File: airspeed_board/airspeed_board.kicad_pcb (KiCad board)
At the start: 2 copper layers, 6 parts, among them J1 BME280, J2 ADXL345, J3 MPXV5002DP, U1 ESP32-C3_SUPERMINI, U2 XGZP6897D_1, U3 XGZP6897D_2

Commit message: updated board layout
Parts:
- removed J3: MPXV5002DP, Connector_PinHeader_2.54mm:PinHeader_1x03_P2.54mm_Vertical
- added C1: 0.1uF, Capacitor_SMD:C_0805_2012Metric, F.Cu at (147.0, 80.3)
- J1: moved to B.Cu
- moved U3 14.9 mm to (138.9, 71.1), turned to 0 degrees
- moved J2 13.8 mm to (168.3, 76.8)
- moved U2 10.0 mm to (138.9, 59.2), turned to 0 degrees
- moved U1 4.66 mm to (138.9, 65.4), turned to 180 degrees
- moved J1 4.47 mm to (150.2, 55.6), turned to -90 degrees
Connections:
- J1 pad 1: unconnected-(J1-Pin_1-Pad1) -> 3.3V
- J1 pad 2: unconnected-(J1-Pin_2-Pad2) -> GND
- J1 pad 3: unconnected-(J1-Pin_3-Pad3) -> SCL
- J1 pad 4: unconnected-(J1-Pin_4-Pad4) -> SDA
- J2 pad 1: unconnected-(J2-Pin_1-Pad1) -> GND
- J2 pad 2: unconnected-(J2-Pin_2-Pad2) -> 3.3V
- J2 pad 7: unconnected-(J2-Pin_7-Pad7) -> SDA
- J2 pad 8: unconnected-(J2-Pin_8-Pad8) -> SCL
- U1 pad 5V: unconnected-(U1-Pad5V) -> 5V
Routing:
- net 3.3V: track 14.9 -> 81.5 mm
- net SCL: track 17.8 -> 62.5 mm, vias 0 -> 1
- net SDA: track 20.6 -> 51.2 mm, vias 0 -> 1
- net GND: track 26.9 -> 0.00 mm
- added copper zone on B.Cu, net GND
- added copper zone on F.Cu, net GND
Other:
- board outline added: 49.5 x 31.2 mm

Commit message: updates to pcb
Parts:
- removed C1: 0.1uF, Capacitor_SMD:C_0805_2012Metric
- moved U3 13.0 mm to (138.9, 58.2)
- moved U2 11.4 mm to (138.9, 70.6)
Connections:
- U1 pad 20: unconnected-(U1-GPIO20-Pad20) -> SDA2
- U1 pad 21: unconnected-(U1-GPIO21-Pad21) -> SCL2
- U3 pad 6: SDA -> SDA2
- U3 pad 7: SCL -> SCL2
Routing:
- net SCL2: track 0.00 -> 19.7 mm
- net SDA: track 51.2 -> 32.3 mm, vias 1 -> 0
- net SCL: track 62.5 -> 47.7 mm, vias 1 -> 0
- net 3.3V: track 81.5 -> 73.5 mm, vias 0 -> 1
- net SDA2: track 0.00 -> 4.41 mm
- removed copper zone on F.Cu, net GND
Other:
- board size 49.5 x 31.2 mm -> 47 x 29.7 mm
- board text added: "SCL"
- board text added: "SCL2"
- board text added: "SDA"
- board text added: "SDA2"
- board text added: "niig:2024.03.04"
- board text added: "velometa.com/airspeed"

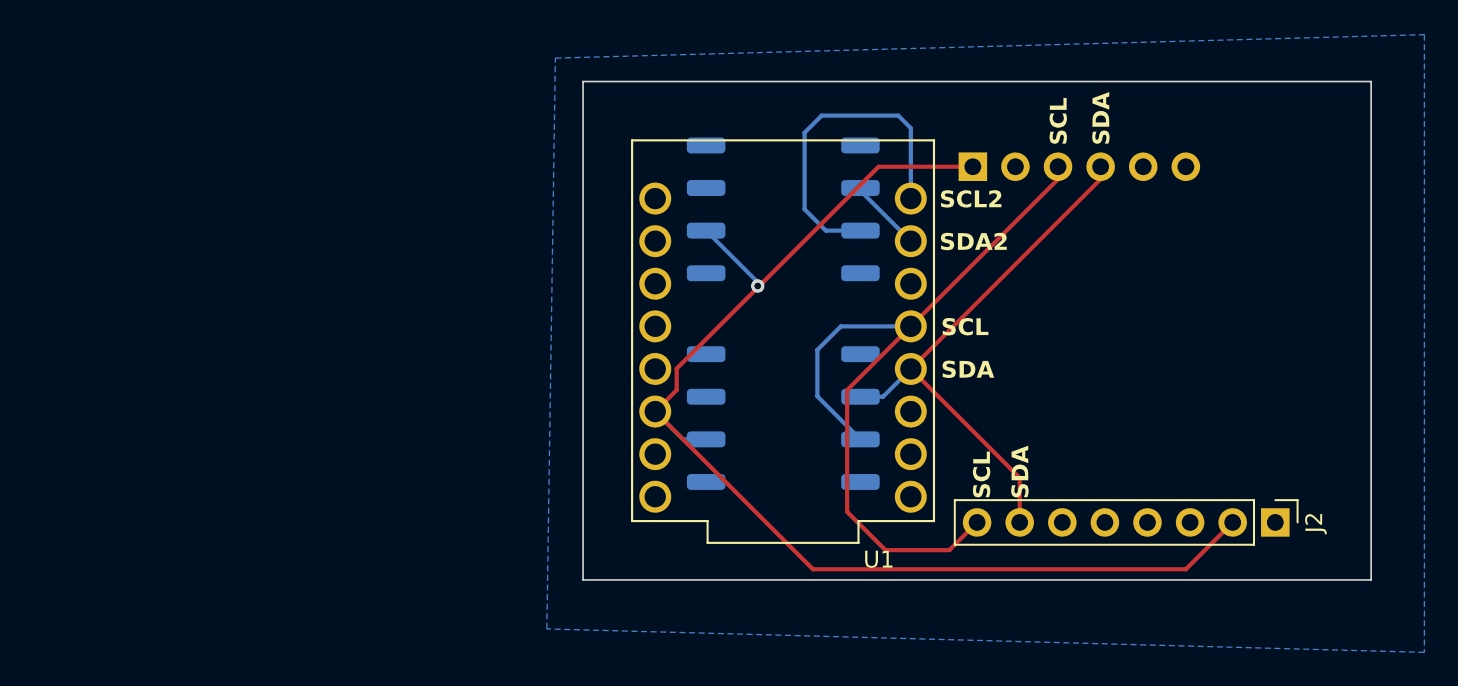
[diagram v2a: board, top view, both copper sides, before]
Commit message: update fix the power for bme and battery connector
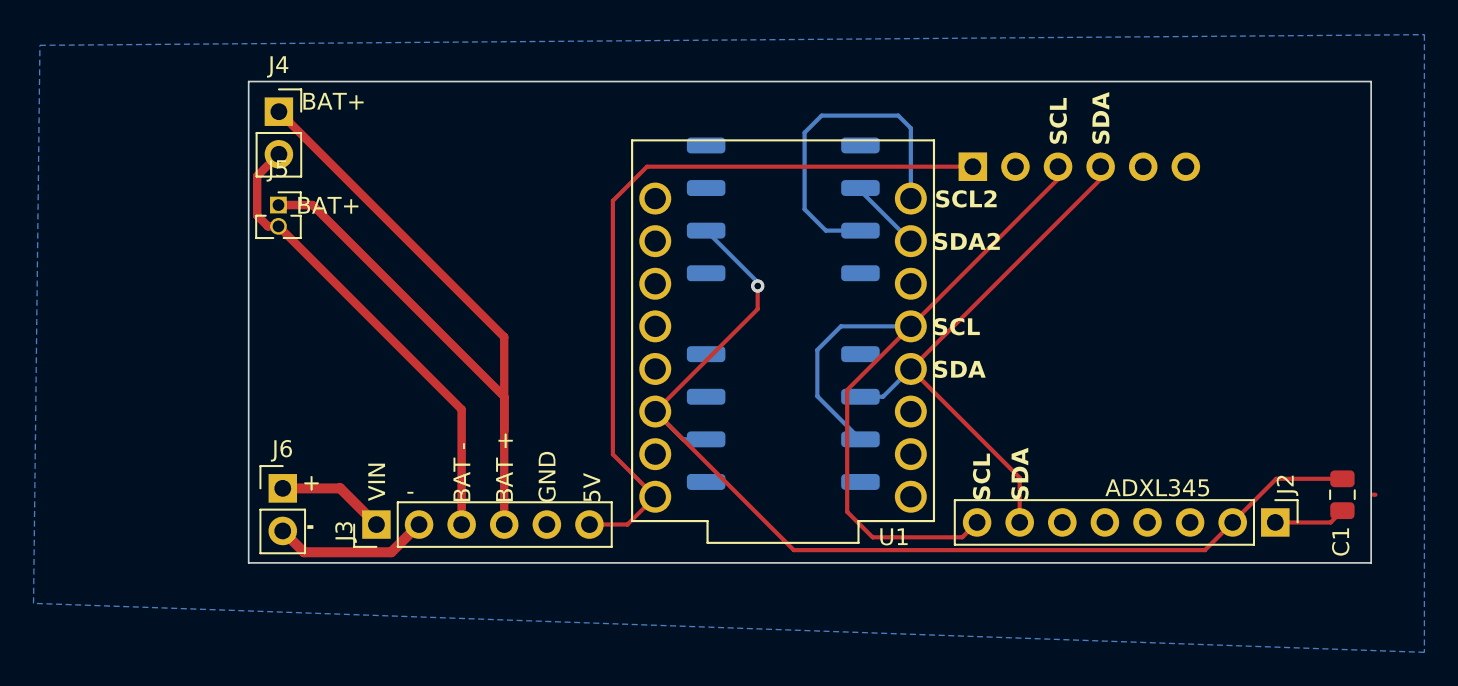
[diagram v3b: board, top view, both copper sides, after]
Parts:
- added C1: 0.1uF, Capacitor_SMD:C_0805_2012Metric, F.Cu at (172.3, 75.2)
- added J3: MH CD42, Connector_PinHeader_2.54mm:PinHeader_1x06_P2.54mm_Vertical, F.Cu at (114.7, 77.0)
- added J4: Battery, Connector_PinSocket_2.54mm:PinSocket_1x02_P2.54mm_Vertical, F.Cu at (108.9, 52.3)
- added J5: Battery, Connector_PinSocket_1.27mm:PinSocket_1x02_P1.27mm_Vertical, F.Cu at (108.8, 57.9)
- added J6: Power In, Connector_PinHeader_2.54mm:PinHeader_1x02_P2.54mm_Vertical, F.Cu at (109.1, 74.8)
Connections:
- J1 pad 1: 3.3V -> 5V
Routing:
- net BAT+: track 0.00 -> 56.4 mm
- net 5V: track 0.00 -> 45.6 mm
- net BAT-: track 0.00 -> 28.0 mm
- net VGND: track 0.00 -> 9.34 mm
- net 3.3V: track 73.5 -> 64.5 mm
- net VIN: track 0.00 -> 6.48 mm
- net GND: track 0.00 -> 4.29 mm
- net SCL: track 47.7 -> 47.1 mm
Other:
- board size 47 x 29.7 mm -> 66.9 x 28.7 mm
- board text added: "+"
- board text added: "-"
- board text added: "5V"
- board text added: "BAT +"
- board text added: "BAT -"
- board text added: "BAT+"
- board text added: "GND"
- board text added: "VIN"
- board text added: "niig:2024.03.23"
- board text removed: "niig:2024.03.04"
